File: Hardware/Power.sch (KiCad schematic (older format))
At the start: 20 parts, among them U7 LTC3129-SOP, U8 AOZ1280

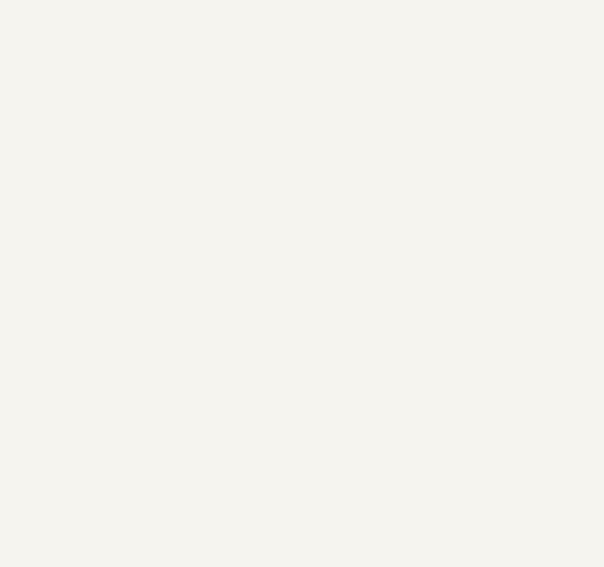
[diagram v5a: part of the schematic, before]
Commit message: Add shielding fingers to bottom of board
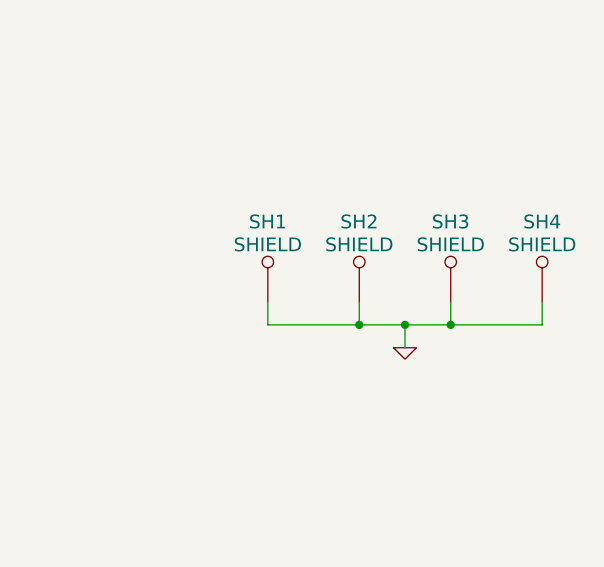
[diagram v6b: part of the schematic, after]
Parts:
- added SH1, SH2, SH3, SH4: SHIELD, EMI-TE-155157X, symbol TP
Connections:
- net GND: now also SH1.1, SH2.1, SH3.1, SH4.1
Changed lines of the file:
@@
 Sheet 5 5
 Title ""
-Date "26 dec 2013"
+Date "27 dec 2013"
 Rev ""
 Comp ""
@@
 $EndDescr
 $Comp
-L VCOM #PWR84
+L VCOM #PWR85
 U 1 1 5241F463
 P 1300 2000
-F 0 "#PWR84" H 1300 2200 40  0001 C CNN
+F 0 "#PWR85" H 1300 2200 40  0001 C CNN
 F 1 "VCOM" H 1300 2150 40  0000 C CNN
 F 2 "" H 1300 2000 60  0000 C CNN
@@
 Connection ~ 1700 1600
 $Comp
-L VCOM #PWR88
+L VCOM #PWR89
 U 1 1 52455206
 P 2400 4800
-F 0 "#PWR88" H 2400 5000 40  0001 C CNN
+F 0 "#PWR89" H 2400 5000 40  0001 C CNN
 F 1 "VCOM" H 2400 4950 40  0000 C CNN
 F 2 "" H 2400 4800 60  0000 C CNN
@@
 Bst
 Connection ~ 3000 4500
+$Comp
+L TP SH1
+U 1 1 52BCE4A7
+P 7600 3400
+F 0 "SH1" H 7600 3750 60  0000 C CNN
+F 1 "SHIELD" H 7600 3650 60  0000 C CNN
+F 2 "EMI-TE-155157X" H 7600 3400 60  0001 C CNN
+F 3 "~" H 7600 3400 60  0000 C CNN
+F 4 "TE" H 7600 3400 60  0001 C CNN "MFR Name"
+F 5 "1551573-5" H 7600 3400 60  0001 C CNN "MFR Part No"
+F 6 "A104054CT-ND" H 7600 3400 60  0001 C CNN "Distributor Part No"
+	1    7600 3400
+	1    0    0    -1
+$EndComp
+$Comp
+L TP SH2
+U 1 1 52BCE50F
+P 8000 3400
+F 0 "SH2" H 8000 3750 60  0000 C CNN
+F 1 "SHIELD" H 8000 3650 60  0000 C CNN
+F 2 "EMI-TE-155157X" H 8000 3400 60  0001 C CNN
+F 3 "~" H 8000 3400 60  0000 C CNN
+F 4 "TE" H 8000 3400 60  0001 C CNN "MFR Name"
+F 5 "1551573-5" H 8000 3400 60  0001 C CNN "MFR Part No"
+F 6 "A104054CT-ND" H 8000 3400 60  0001 C CNN "Distributor Part No"
+	1    8000 3400
+	1    0    0    -1
+$EndComp
+$Comp
+L TP SH3
+U 1 1 52BCE518
+P 8400 3400
+F 0 "SH3" H 8400 3750 60  0000 C CNN
+F 1 "SHIELD" H 8400 3650 60  0000 C CNN
+F 2 "EMI-TE-155157X" H 8400 3400 60  0001 C CNN
+F 3 "~" H 8400 3400 60  0000 C CNN
+F 4 "TE" H 8400 3400 60  0001 C CNN "MFR Name"
+F 5 "1551573-5" H 8400 3400 60  0001 C CNN "MFR Part No"
+F 6 "A104054CT-ND" H 8400 3400 60  0001 C CNN "Distributor Part No"
+	1    8400 3400
+	1    0    0    -1
+$EndComp
+$Comp
+L TP SH4
+U 1 1 52BCE521
+P 8800 3400
+F 0 "SH4" H 8800 3750 60  0000 C CNN
+F 1 "SHIELD" H 8800 3650 60  0000 C CNN
+F 2 "EMI-TE-155157X" H 8800 3400 60  0001 C CNN
+F 3 "~" H 8800 3400 60  0000 C CNN
+F 4 "TE" H 8800 3400 60  0001 C CNN "MFR Name"
+F 5 "1551573-5" H 8800 3400 60  0001 C CNN "MFR Part No"
+F 6 "A104054CT-ND" H 8800 3400 60  0001 C CNN "Distributor Part No"
+	1    8800 3400
+	1    0    0    -1
+$EndComp
+$Comp
+L GND #PWR096
+U 1 1 52BCE529
+P 8200 3600
+F 0 "#PWR096" H 8200 3600 30  0001 C CNN
+F 1 "GND" H 8200 3530 30  0001 C CNN
+F 2 "" H 8200 3600 60  0000 C CNN
+F 3 "" H 8200 3600 60  0000 C CNN
+	1    8200 3600
+	1    0    0    -1
+$EndComp
+Wire Wire Line
+	7600 3400 7600 3500
+Wire Wire Line
+	7600 3500 8800 3500
+Wire Wire Line
+	8800 3500 8800 3400
+Wire Wire Line
+	8400 3400 8400 3500
+Connection ~ 8400 3500
+Wire Wire Line
+	8000 3400 8000 3500
+Connection ~ 8000 3500
+Wire Wire Line
+	8200 3600 8200 3500
+Connection ~ 8200 3500
 $EndSCHEMATC
